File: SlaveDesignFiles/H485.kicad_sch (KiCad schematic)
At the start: 22 parts

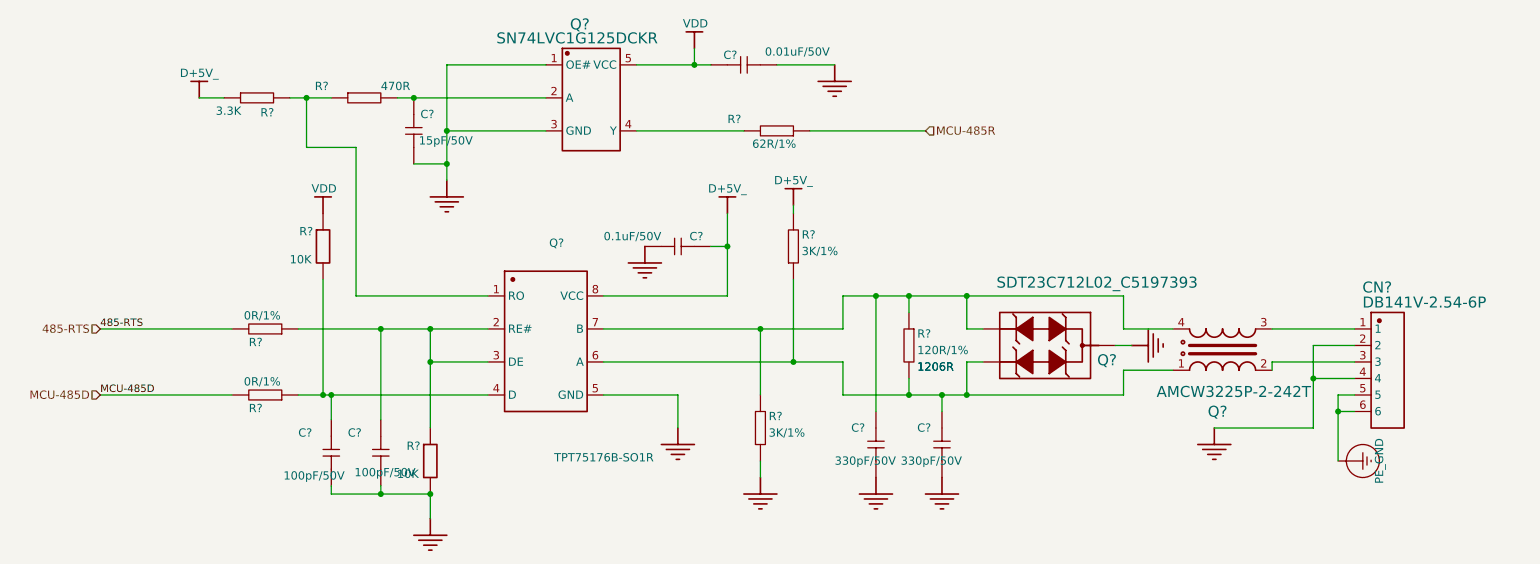
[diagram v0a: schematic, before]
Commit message: 1. 在USB处，修改了type-c5V输入的定义，添加了二极管；2. 将CJA1117B-3.3替换为AMS1117-3.3；3. 分配了testpoint的封装；4. 修改了H485，can插件的PE_GNG引脚定义。
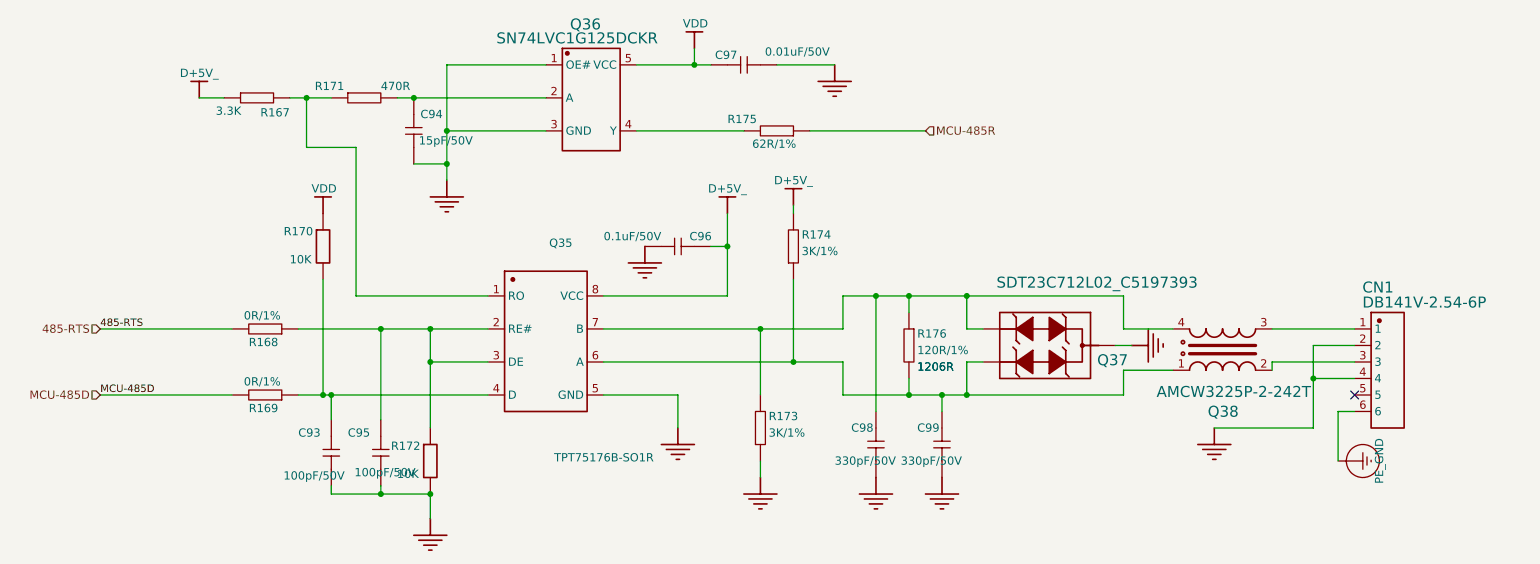
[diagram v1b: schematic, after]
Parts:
- gave numbers to parts that had none: 22
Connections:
- net PE_GND: no longer CN1.5
- no-connect marks 0 -> 1

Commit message: Fix bugs in PWM subsheet
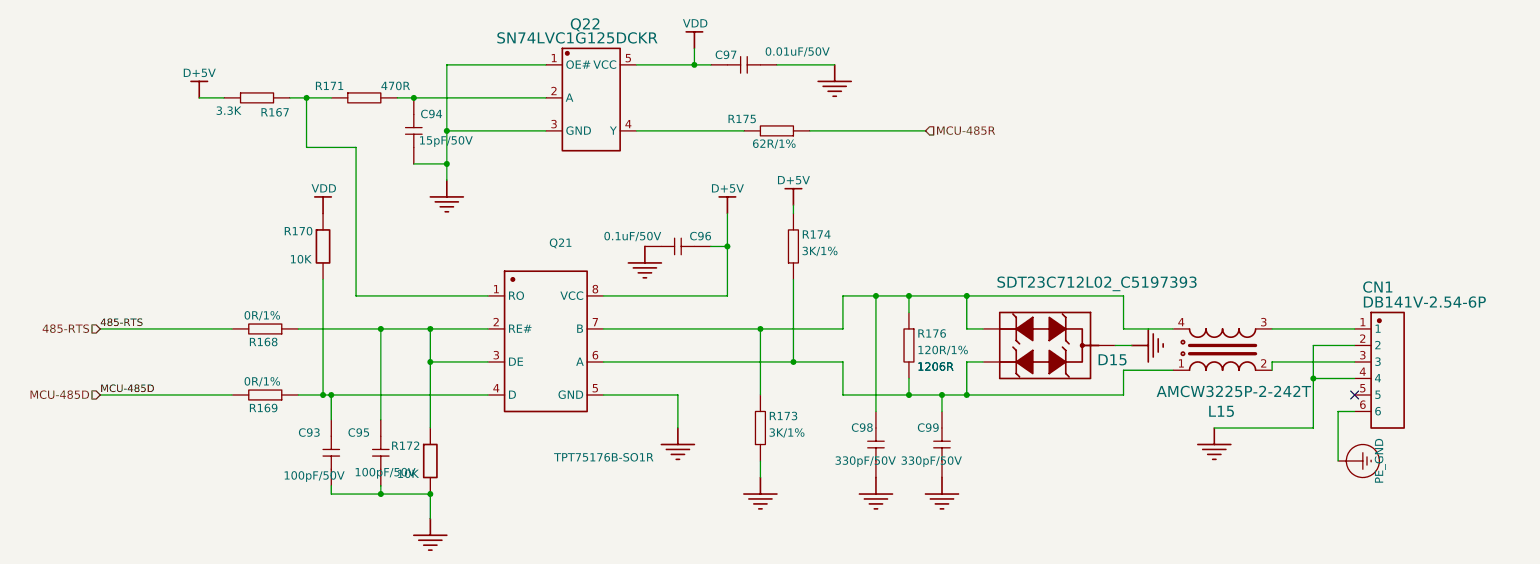
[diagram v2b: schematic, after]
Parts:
- renumbered Q37 to D15, Q38 to L15, Q35 to Q21, Q36 to Q22
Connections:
- net D+5V_ renamed D+5V
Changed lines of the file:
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@@
 		(on_board yes)
 		(dnp no)
-		(property "Reference" "Q36"
+		(property "Reference" "Q22"
 			(at 102.7684 41.0337 0)
 			(effects
@@
 			(project "sheet1"
 				(path "/54840d93-b842-4275-b1cb-4ec5510cbfff/032c7b12-abe7-49c0-bf87-4f9652e41bfa"
-					(reference "Q40")
+					(reference "Q24")
 					(unit 1)
 				)
 				(path "/54840d93-b842-4275-b1cb-4ec5510cbfff/48c092ad-bff6-4c71-add6-c61e4021ba6b"
-					(reference "Q36")
+					(reference "Q22")
 					(unit 1)
 				)
@@
 		(on_board yes)
 		(dnp no)
-		(property "Reference" "Q38"
+		(property "Reference" "L15"
 			(at 200.914 102.616 0)
 			(effects
@@
 			(project "sheet1"
 				(path "/54840d93-b842-4275-b1cb-4ec5510cbfff/032c7b12-abe7-49c0-bf87-4f9652e41bfa"
-					(reference "Q42")
+					(reference "L16")
 					(unit 0)
 				)
 				(path "/54840d93-b842-4275-b1cb-4ec5510cbfff/48c092ad-bff6-4c71-add6-c61e4021ba6b"
-					(reference "Q38")
+					(reference "L15")
 					(unit 0)
 				)
@@
 			)
 		)
-		(property "Value" "D+5V_"
+		(property "Value" "D+5V"
 			(at 137.16 66.04 0)
 			(effects
@@
 		(on_board yes)
 		(dnp no)
-		(property "Reference" "Q35"
+		(property "Reference" "Q21"
 			(at 99.568 74.93 0)
 			(effects
@@
 			(project "sheet1"
 				(path "/54840d93-b842-4275-b1cb-4ec5510cbfff/032c7b12-abe7-49c0-bf87-4f9652e41bfa"
-					(reference "Q39")
+					(reference "Q23")
 					(unit 1)
 				)
 				(path "/54840d93-b842-4275-b1cb-4ec5510cbfff/48c092ad-bff6-4c71-add6-c61e4021ba6b"
-					(reference "Q35")
+					(reference "Q21")
 					(unit 1)
 				)
@@
 			)
 		)
-		(property "Value" "D+5V_"
+		(property "Value" "D+5V"
 			(at 45.72 49.53 0)
 			(effects
@@
 			)
 		)
-		(property "Value" "D+5V_"
+		(property "Value" "D+5V"
 			(at 127 67.31 0)
 			(effects
@@
 		(on_board yes)
 		(dnp no)
-		(property "Reference" "Q37"
+		(property "Reference" "D15"
 			(at 183.896 92.71 90)
 			(effects
@@
 			(project "sheet1"
 				(path "/54840d93-b842-4275-b1cb-4ec5510cbfff/032c7b12-abe7-49c0-bf87-4f9652e41bfa"
-					(reference "Q41")
+					(reference "D16")
 					(unit 1)
 				)
 				(path "/54840d93-b842-4275-b1cb-4ec5510cbfff/48c092ad-bff6-4c71-add6-c61e4021ba6b"
-					(reference "Q37")
+					(reference "D15")
 					(unit 1)
 				)
